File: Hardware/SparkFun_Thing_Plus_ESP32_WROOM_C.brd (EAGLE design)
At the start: 22.9 x 58.4 mm, 106 parts, among them J3 QWIIC_RIGHT_ANGLE, J6 microSD, Q2 MBT3904DW1T1, Q3 20V/4.2A/52mΩ/1.4W, U1 MCP73831, U2 ESP-WROOM-32NARROW, U3 AP2112K-3.3, U4 MAX17048, U5 AP2112K-3.3, U6 THINGPLUS_LOGICAL, U7 CH340C

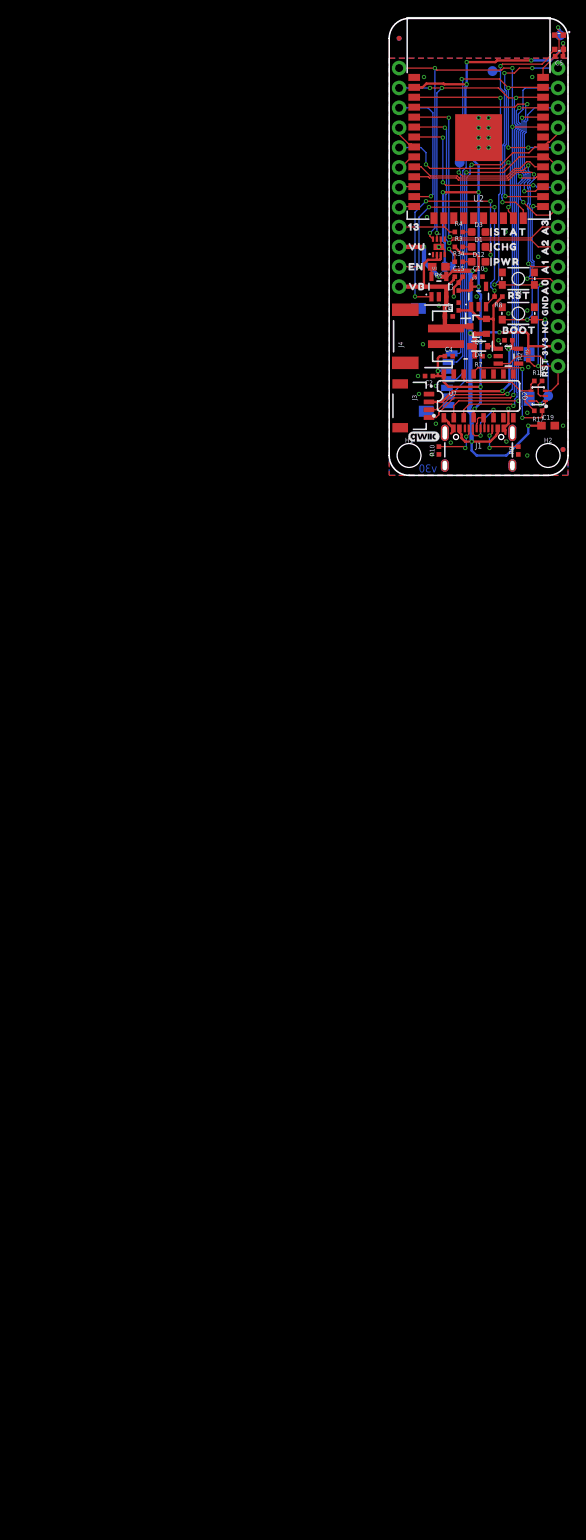
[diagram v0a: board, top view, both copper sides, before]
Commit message: Renamed schematics, replaced parts with sfe lib parts.
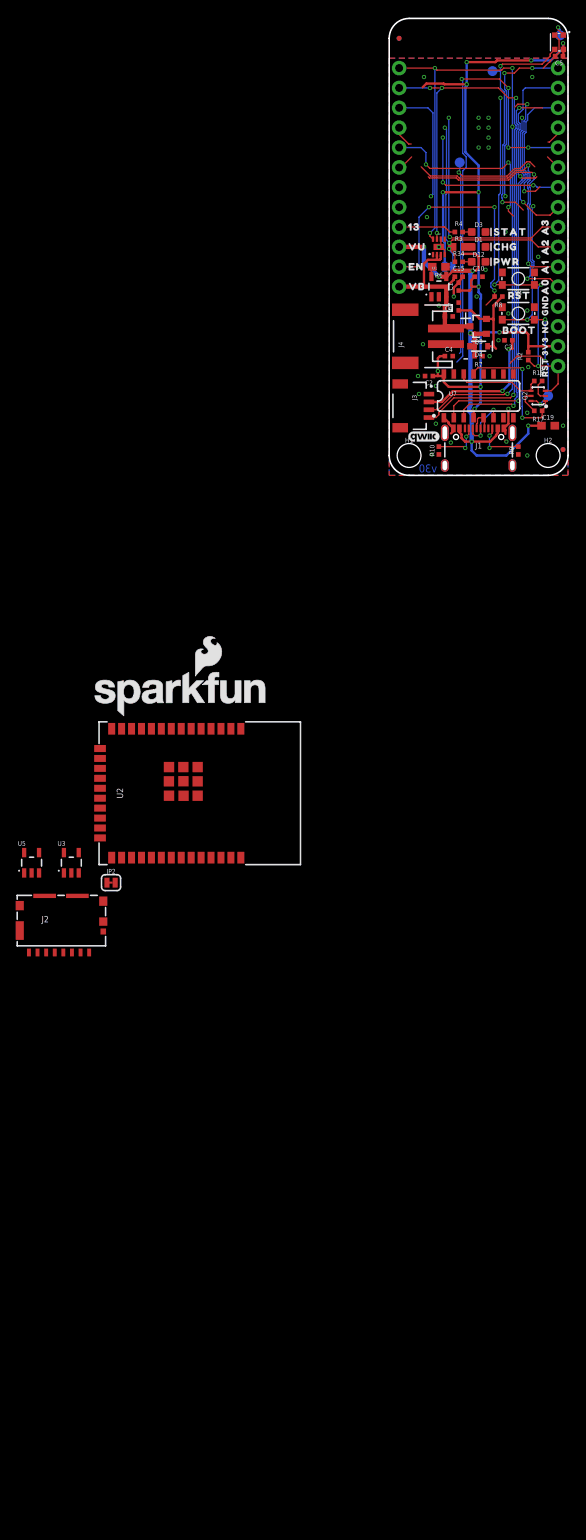
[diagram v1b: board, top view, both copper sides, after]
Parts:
- removed J6: microSD, SparkFun-Connectors:MICRO-SD-SOCKET
- removed U$1: SPARKX-LOGO4, SparkX:SPARKX-MEDIUM
- added J2: MICRO-SDFRICTION, SparkFun-Connectors:MICROSD_TINY
- added JP2: (no value), SparkFun-Jumpers:SMT-JUMPER_2_NC_TRACE_SILK
- added LOGO1: SFE_LOGO_NAME_FLAME.2_INCH, SparkFun-Aesthetics:SFE_LOGO_NAME_FLAME_.2
- J3: value QWIIC_RIGHT_ANGLE -> QWIIC_RA
- R3: value 1k -> 150; device SparkFun-Resistors:0402-TIGHT -> SparkFun-Resistors:0603
- U1: device SparkFun-PowerIC:SOT23-5 -> SparkFun-IC-Power:SOT23-5
- U2: value ESP-WROOM-32NARROW -> ESP-WROOM-3232D-NARROW; device SparkFun-RF:ESP-WROOM-32-NARROW -> SparkFun-RF:ESP-WROOM-32D-NARROW
- U3, U5: value AP2112K-3.3 -> XC6222B331MR-G
- moved U2 92.7 mm to (-25.4, -40.6), turned to 0 degrees
- moved U3 89.2 mm to (-40.6, -49.5)
- moved U5 88.9 mm to (-45.7, -49.5), turned to 0 degrees
- moved U$59 67.3 mm to (33.0, 53.3)
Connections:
- net CHG renamed N$7
- removed net ESP_19/TP_CIPO: J6.DO/DAT0, U2.31, U6.CIPO
- removed net ESP_23/TP_COPI: J6.DI/CMD, U2.37, U6.COPI
- new net ESP_19/TP_POCI: J2.7, U2.31, U6.CIPO
- new net ESP_23/TP_PICO: J2.3, U2.37, U6.COPI
- new net N$4: JP2.1, R3.1
- net 3.3V: now also J2.4; no longer J6.VCC
- net ESP_18/TP_SCK: now also J2.5; no longer J6.SCLK
- net ESP_5/SD_CS: now also J2.2; no longer J6.CS/DAT3
- net GND: now also J2.6, J2.GND1, J2.GND2, J2.GND3, J2.GND4, J2.GND5, J2.GND6, U2.GND1, U2.GNDT1, U2.GNDT2, U2.GNDT3, U2.GNDT4, U2.GNDT5, U2.GNDT6, U2.GNDT7, U2.GNDT8; no longer J6.CD1, J6.GND, J6.GND1, J6.GND3, U2.GND
- net V_USB: now also JP2.2; no longer R3.1
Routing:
- net ESP_23/TP_COPI: track 62.8 -> 0.00 mm, vias 4 -> 0
- net ESP_23/TP_PICO: track 0.00 -> 57.4 mm, vias 0 -> 4
- net ESP_19/TP_CIPO: track 44.4 -> 0.00 mm, vias 1 -> 0
- net ESP_18/TP_SCK: track 41.1 -> 1.91 mm, vias 1 -> 0
- net N$7: track 31.3 -> 0.00 mm, vias 4 -> 0
- net ESP_36/TP_A4: track 33.6 -> 20.8 mm
- net !RESET!: track 60.2 -> 49.3 mm
- net ESP_4/TP_FB: track 27.9 -> 23.2 mm
- net ESP_39/TP_A3: track 34.2 -> 29.9 mm
- net ESP_21/TP_SDA: track 93.7 -> 89.8 mm
- net ESP_34/TP_A2: track 33.4 -> 29.6 mm
- net ESP_35/TP_A5: track 24.4 -> 20.8 mm
- net ESP_22/TP_SCL: track 89.0 -> 85.6 mm
- net ESP_0/QPWR: track 41.3 -> 38.6 mm
- net 3.3V: track 111.9 -> 109.3 mm
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
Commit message: All parts are now from SFE libs.
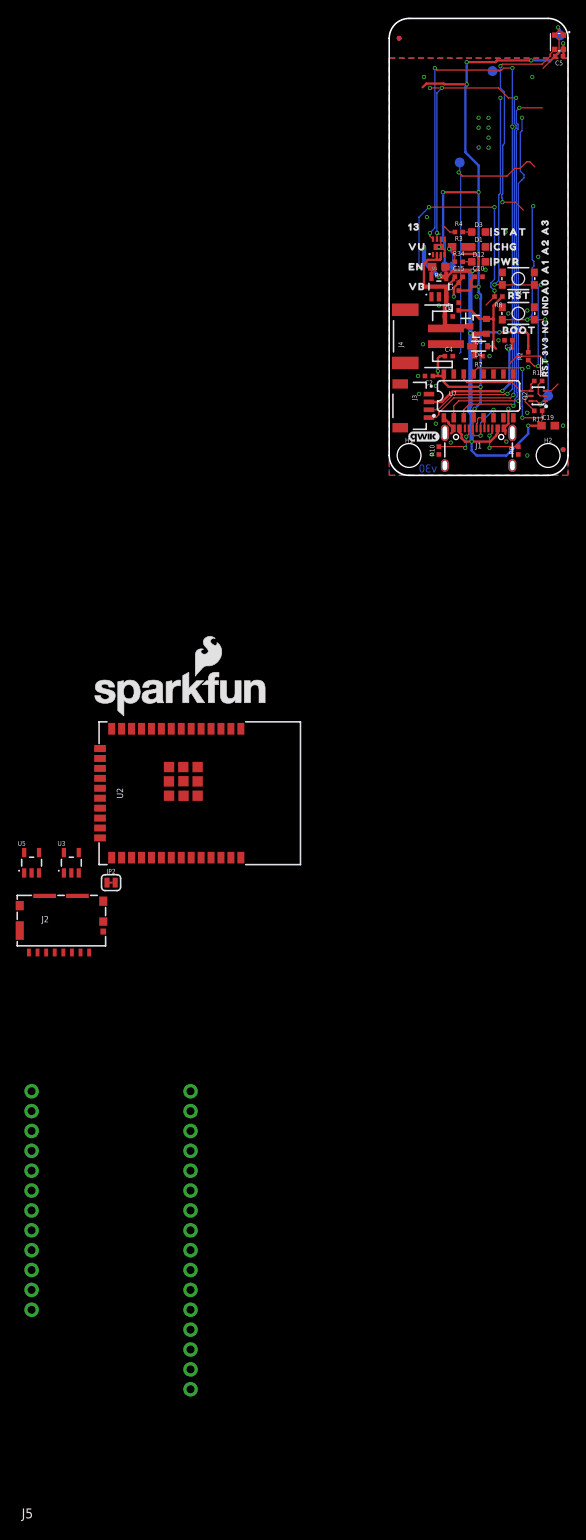
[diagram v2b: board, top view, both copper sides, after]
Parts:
- removed U6: THINGPLUS_LOGICAL, ThingPlus:THINGPLUS_FOOTPRINT
- added J5: THING_PLUS, SparkFun-Boards:THING_PLUS
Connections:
- removed net ESP_12/TP_12: U2.14, U6.12
- removed net ESP_14/TP_7: U2.13, U6.7
- removed net ESP_15/TP_9: U2.23, U6.9
- removed net ESP_27/TP_11: U2.12, U6.11
- removed net ESP_32/TP_8: U2.8, U6.8
- removed net ESP_33/TP_10: U2.9, U6.10
- new net ESP_12/TP_5: J5.4, U2.14
- new net ESP_13/TP_6/LED: J5.3
- new net ESP_14/TP_0: J5.9, U2.13
- new net ESP_15/TP_2: J5.7, U2.23
- new net ESP_27/TP_4: J5.5, U2.12
- new net ESP_32/TP_1: J5.8, U2.8
- new net ESP_33/TP_3: J5.6, U2.9
- net !RESET!: now also J5.28; no longer U6.RST
- net 3.3V: now also J5.27; no longer U6.3V3
- net ESP_13/TP_13/LED: no longer U6.13
- net ESP_16/TP_RX: now also J5.15; no longer U6.RX
- net ESP_17/TP_TX: now also J5.14; no longer U6.TX
- net ESP_18/TP_SCK: now also J5.18; no longer U6.SCK
- net ESP_19/TP_POCI: now also J5.16; no longer U6.CIPO
- net ESP_21/TP_SDA: now also J5.1; no longer U6.SDA
- net ESP_22/TP_SCL: now also J5.2; no longer U6.SCL
- net ESP_23/TP_PICO: now also J5.17; no longer U6.COPI
- net ESP_25/TP_A1: now also J5.23; no longer U6.A1
- net ESP_26/TP_A0: now also J5.24; no longer U6.A0
- net ESP_34/TP_A2: now also J5.22; no longer U6.A2
- net ESP_35/TP_A5: now also J5.19; no longer U6.A5
- net ESP_36/TP_A4: now also J5.20; no longer U6.A4
- net ESP_39/TP_A3: now also J5.21; no longer U6.A3
- net ESP_4/TP_FB: now also J5.13; no longer U6.FREEBIE
- net GND: now also J5.25; no longer U6.GND
- net TP_EN: now also J5.11; no longer U6.EN
- net V_BATT: now also J5.12; no longer U6.V_BATT
- net V_USB: now also J5.10; no longer U6.V_USB
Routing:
- net ESP_23/TP_PICO: track 57.4 -> 0.00 mm, vias 4 -> 0
- net ESP_26/TP_A0: track 32.6 -> 0.00 mm, vias 2 -> 0
- net ESP_25/TP_A1: track 31.8 -> 0.00 mm, vias 2 -> 0
- net ESP_39/TP_A3: track 29.9 -> 0.00 mm, vias 2 -> 0
- net ESP_34/TP_A2: track 29.6 -> 0.00 mm, vias 2 -> 0
- net ESP_15/TP_9: track 23.6 -> 0.00 mm, vias 3 -> 0
- net ESP_4/TP_FB: track 23.2 -> 0.00 mm, vias 3 -> 0
- net ESP_35/TP_A5: track 20.8 -> 0.00 mm, vias 3 -> 0
- net ESP_36/TP_A4: track 20.8 -> 0.00 mm, vias 2 -> 0
- net ESP_17/TP_TX: track 18.4 -> 0.00 mm, vias 1 -> 0
- net ESP_16/TP_RX: track 16.9 -> 0.00 mm, vias 1 -> 0
- net ESP_14/TP_7: track 15.4 -> 0.00 mm, vias 1 -> 0
- net ESP_13/TP_13/LED: track 7.38 -> 1.67 mm
- net !RESET!: track 49.3 -> 44.4 mm
- net ESP_21/TP_SDA: track 89.8 -> 85.3 mm
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
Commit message: Placed all new components, pinned out PTHs.
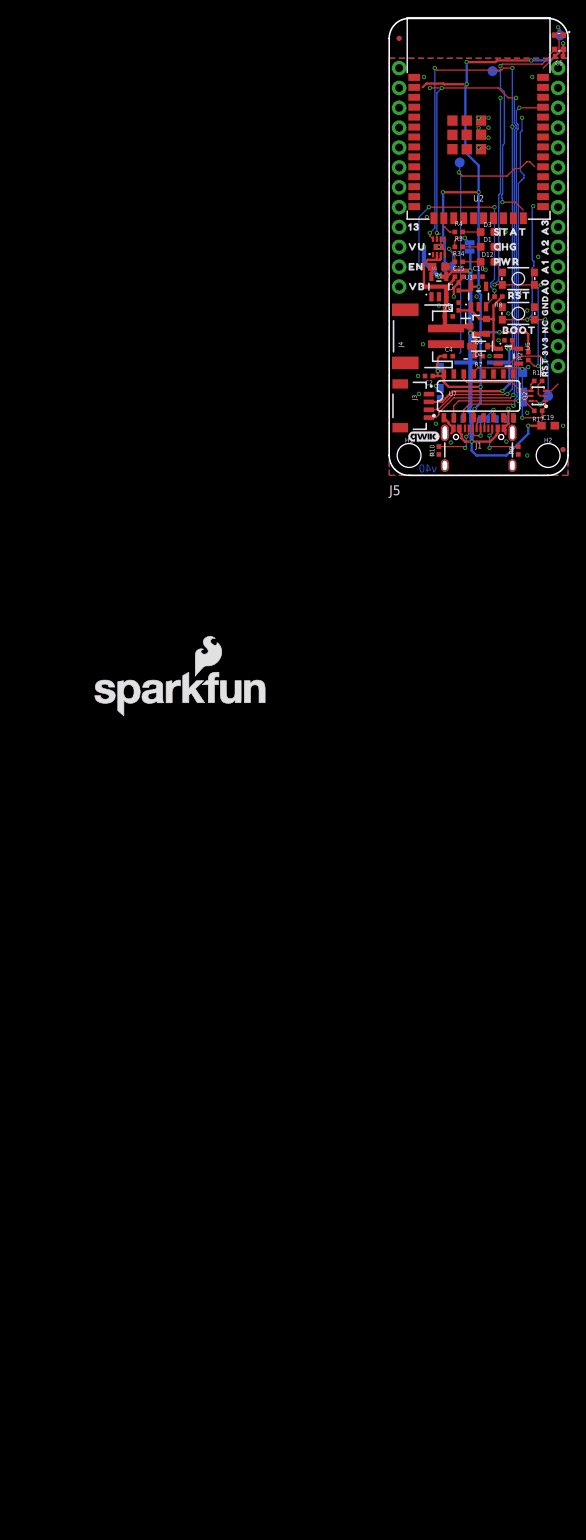
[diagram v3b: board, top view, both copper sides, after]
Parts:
- R3: value 150 -> 1k; device SparkFun-Resistors:0603 -> SparkFun-Resistors:0402-TIGHT
- moved J5 139.0 mm to (0.00, 0.00)
- moved JP2 93.3 mm to (10.3, 29.2), flipped to the bottom, turned to 270 degrees
- moved U2 92.7 mm to (11.4, 44.5), turned to 90 degrees
- moved U3 89.2 mm to (11.4, 22.9)
- moved U5 88.9 mm to (15.2, 15.2), turned to 270 degrees
- moved J2 86.8 mm to (11.8, 11.0), flipped to the bottom
- moved D1 1.14 mm to (12.6, 29.2)
- moved D12 1.14 mm to (12.6, 27.3)
- moved D3 1.14 mm to (12.6, 31.1)
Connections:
- net ESP_33/TP_3 renamed ESP_33/TP_6
- removed net ESP_12/TP_5: J5.4, U2.14
- removed net ESP_13/TP_13/LED: R4.1, U2.16
- removed net ESP_13/TP_6/LED: J5.3
- removed net ESP_14/TP_0: J5.9, U2.13
- removed net ESP_15/TP_2: J5.7, U2.23
- removed net ESP_27/TP_4: J5.5, U2.12
- removed net ESP_32/TP_1: J5.8, U2.8
- new net ESP_12/TP_8: J5.8, U2.14
- new net ESP_13/TP_9/LED: J5.9, R4.1, U2.16
- new net ESP_14/TP_3: J5.3, U2.13
- new net ESP_15/TP_5: J5.5, U2.23
- new net ESP_27/TP_7: J5.7, U2.12
- new net ESP_32/TP_4: J5.4, U2.8
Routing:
- net N$4: track 0.00 -> 3.09 mm, vias 0 -> 1
- net V_USB: track 61.4 -> 58.9 mm
- net ESP_13/TP_9/LED: track 0.00 -> 1.67 mm
- net ESP_13/TP_13/LED: track 1.67 -> 0.00 mm
- net CHG_LED: track 0.81 -> 2.31 mm
- net N$30: track 1.16 -> 2.31 mm
- net N$2: track 1.16 -> 2.31 mm
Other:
- board text added: "v40"
- board text removed: "v30"

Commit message: End of day commit, placed uSD conn and began routing.
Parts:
- moved LOGO2 0.92 mm to (21.1, 8.13)
- moved J2 0.45 mm to (12.1, 10.7)
- moved U7 0.15 mm to (11.4, 10.0)
- moved J1 0.15 mm to (11.4, 6.20)
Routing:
- net V_USB: track 58.9 -> 35.4 mm, vias 6 -> 4
- net !RESET!: track 44.4 -> 60.2 mm
- net QWIIC_PWR: track 17.4 -> 1.62 mm, vias 2 -> 1
- net CH340-RX: track 49.4 -> 34.5 mm, vias 2 -> 1
- net CH340-TX: track 47.0 -> 33.3 mm, vias 2 -> 1
- net 3.3V: track 105.4 -> 93.2 mm, vias 11 -> 9
- net ESP_22/TP_SCL: track 81.7 -> 71.3 mm, vias 5 -> 4
- net CH340-DTR: track 17.8 -> 8.34 mm, vias 2 -> 0
- net ESP_21/TP_SDA: track 85.3 -> 77.2 mm, vias 5 -> 4
- net ESP_13/TP_9/LED: track 1.67 -> 8.51 mm
- net GND: track 17.5 -> 13.7 mm, vias 34 -> 21
- net ESP_32/TP_4: track 0.00 -> 3.45 mm
- net V_BATT: track 19.9 -> 23.0 mm
- net ESP_33/TP_6: track 0.00 -> 2.48 mm
- net ESP_27/TP_7: track 0.00 -> 1.96 mm
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
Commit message: Initial reroute complete.
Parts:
- TP1, TP2, TP3, TP4: value (none) -> TEST-POINT3X5
- moved R18 0.80 mm to (18.6, 11.4)
- moved C3 0.76 mm to (16.0, 17.3)
- moved C2 0.55 mm to (5.33, 12.2), turned to 270 degrees
- moved Q2 0.51 mm to (19.1, 9.65)
- moved R17 0.51 mm to (19.1, 7.75)
- moved R2 0.51 mm to (18.3, 15.2)
- moved R34 0.30 mm to (9.17, 27.2)
- moved R3 0.25 mm to (9.14, 29.2)
- moved C4 0.13 mm to (7.49, 15.3)
- moved C19 0.13 mm to (20.3, 6.22)
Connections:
- net ESP_0/QPWR: now also TP1.1; no longer TP1.P$1
- net ESP_2/RGB_DI: now also TP3.1; no longer TP3.P$1
- net ESP_5/SD_CS: now also TP4.1; no longer TP4.P$1
- net N$3: now also TP2.1; no longer TP2.P$1
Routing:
- net ESP_23/TP_PICO: track 0.00 -> 53.9 mm, vias 0 -> 5
- net ESP_18/TP_SCK: track 0.00 -> 49.0 mm, vias 0 -> 3
- net ESP_19/TP_POCI: track 0.00 -> 46.4 mm, vias 0 -> 1
- net V_USB: track 35.4 -> 77.1 mm, vias 4 -> 8
- net ESP_34/TP_A2: track 0.00 -> 34.0 mm, vias 0 -> 1
- net ESP_4/TP_FB: track 0.00 -> 33.0 mm, vias 0 -> 2
- net ESP_39/TP_A3: track 0.00 -> 31.5 mm, vias 0 -> 1
- net ESP_16/TP_RX: track 0.00 -> 30.3 mm, vias 0 -> 3
- net ESP_36/TP_A4: track 0.00 -> 29.9 mm, vias 0 -> 1
- net ESP_26/TP_A0: track 0.00 -> 29.6 mm
- net ESP_17/TP_TX: track 0.00 -> 28.3 mm, vias 0 -> 3
- net ESP_25/TP_A1: track 0.00 -> 27.9 mm
- net 3.3V: track 93.2 -> 115.7 mm, vias 9 -> 11
- net ESP_22/TP_SCL: track 71.3 -> 93.8 mm, vias 4 -> 5
- net ESP_15/TP_5: track 0.00 -> 22.1 mm, vias 0 -> 1
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
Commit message: Completed Board update pre-DR.
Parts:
- removed U$103: (no value), output:ESP320
- removed U$104: (no value), output:THING1
- removed U$105: (no value), output:PLUS2
- removed U$57: (no value), output:#4#0
- removed U$62: (no value), output:#23#COPI#0
- removed U$82: (no value), output:#19#CIPO#0
- added U$1: (no value), SparkFun-Aesthetics:SFE_LOGO_FLAME_STOP_.1
- added U$2: (no value), output:#23#PICO#0
- added U$3: (no value), output:#19#POCI#0
- added U$4: (no value), output:#4#FREE#0
- added U$5: (no value), output:#CHG_LED#0
- added U$6: (no value), output:ESP32#WROOM0
- added U$7: (no value), output:THING_PLUS_C0
- LOGO1: value SFE_LOGO_NAME_FLAME.2_INCH -> SFE_LOGO_NAME_FLAME.1_INCH; device SparkFun-Aesthetics:SFE_LOGO_NAME_FLAME_.2 -> SparkFun-Aesthetics:SFE_LOGO_NAME_FLAME_.1
- moved LOGO1 60.5 mm to (11.2, 19.3), flipped to the bottom
- moved U$25 1.40 mm to (16.4, 27.3)
- moved U$24 1.37 mm to (16.2, 29.2)
- moved U$26 1.35 mm to (16.8, 31.1)
- moved C3 0.20 mm to (16.0, 17.5)
- moved U5 0.20 mm to (15.2, 15.4)
- moved C1 0.18 mm to (8.84, 24.0)
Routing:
- net ESP_25/TP_A1: track 27.9 -> 26.6 mm
- net ESP_26/TP_A0: track 29.6 -> 28.4 mm
- net GND: vias 110 -> 119
